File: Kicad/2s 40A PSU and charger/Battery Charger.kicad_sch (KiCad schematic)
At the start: 42 parts

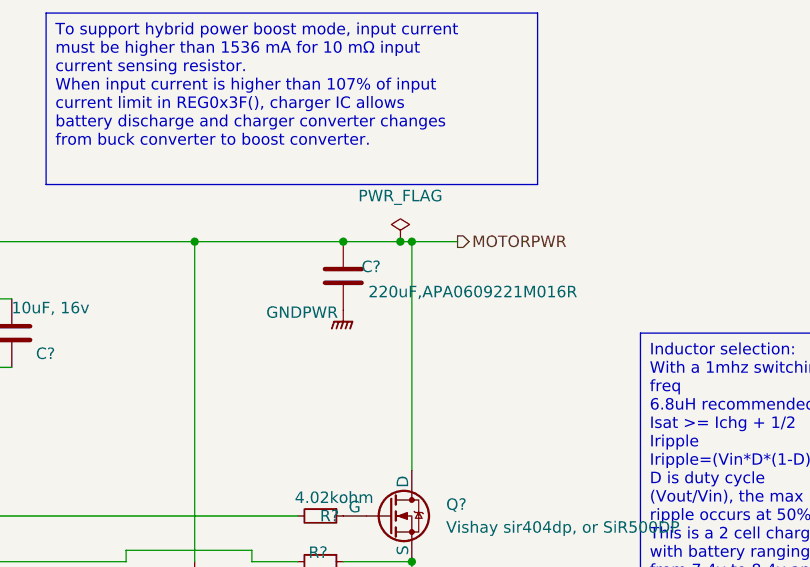
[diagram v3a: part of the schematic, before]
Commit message: Add proper ESD protection and pulldowns for USB-C
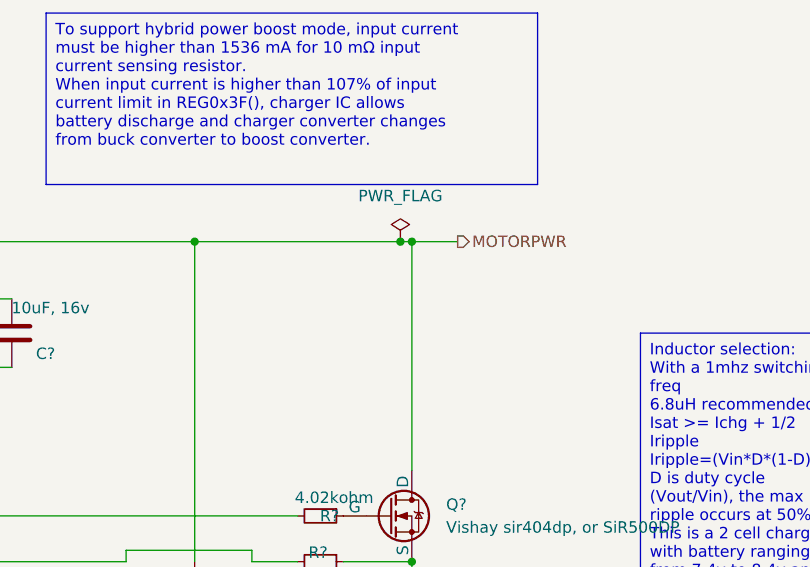
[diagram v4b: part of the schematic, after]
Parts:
- removed C?: 220uF,APA0609221M016R, Capacitor_SMD:CP_Elec_6.3x9.9, symbol Device:C
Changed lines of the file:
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@@
 	)
 	(junction
-		(at 193.04 54.61)
-		(diameter 0)
-		(color 0 0 0 0)
-	)
-	(junction
 		(at 200.66 107.95)
 		(diameter 0)
@@
 	(wire
 		(pts
-			(xy 176.53 54.61) (xy 193.04 54.61)
+			(xy 176.53 54.61) (xy 199.39 54.61)
 		)
 		(stroke
@@
 	(wire
 		(pts
-			(xy 199.39 54.61) (xy 193.04 54.61)
-		)
-		(stroke
-			(width 0)
-			(type default)
-		)
-	)
-	(wire
-		(pts
 			(xy 111.76 107.95) (xy 90.17 107.95)
 		)
@@
 	)
 	(symbol
-		(lib_id "power:GNDPWR")
-		(at 193.04 62.23 0)
-		(unit 1)
-		(exclude_from_sim no)
-		(in_bom yes)
-		(on_board yes)
-		(dnp no)
-		(property "Reference" "#PWR?"
-			(at 193.04 67.31 0)
-			(effects
-				(font
-					(size 1.27 1.27)
-				)
-				(hide yes)
-			)
-		)
-		(property "Value" "GNDPWR"
-			(at 188.468 62.484 0)
-			(effects
-				(font
-					(size 1.27 1.27)
-				)
-			)
-		)
-		(property "Footprint" ""
-			(at 193.04 63.5 0)
-			(effects
-				(font
-					(size 1.27 1.27)
-				)
-				(hide yes)
-			)
-		)
-		(property "Datasheet" ""
-			(at 193.04 63.5 0)
-			(effects
-				(font
-					(size 1.27 1.27)
-				)
-				(hide yes)
-			)
-		)
-		(property "Description" "Power symbol creates a global label with name \"GNDPWR\" , global ground"
-			(at 193.04 62.23 0)
-			(effects
-				(font
-					(size 1.27 1.27)
-				)
-				(hide yes)
-			)
-		)
-		(pin "1"
-		)
-		(instances
-			(project "Battery Charger"
-				(path "/a7feb2bd-883b-459c-b24f-35371efba833"
-					(reference "#PWR?")
-					(unit 1)
-				)
-			)
-			(project "2s 40A PSU and charger"
-				(path "/eb3f183d-8bb1-43a5-a363-092ed67891e3/51a1bb53-ba94-4dbc-a00c-ce32ffc237e4"
-					(reference "#PWR06")
-					(unit 1)
-				)
-			)
-		)
-	)
-	(symbol
 		(lib_id "Device:R_Small")
 		(at 190.5 85.09 270)
@@
 					(unit 1)
 				)
-			)
-		)
-	)
-	(symbol
-		(lib_id "Device:C")
-		(at 193.04 58.42 0)
-		(unit 1)
-		(exclude_from_sim no)
-		(in_bom yes)
-		(on_board yes)
-		(dnp no)
-		(property "Reference" "C?"
-			(at 195.072 57.404 0)
-			(effects
-				(font
-					(size 1.27 1.27)
-				)
-				(justify left)
-			)
-		)
-		(property "Value" "220uF,APA0609221M016R"
-			(at 195.834 60.198 0)
-			(effects
-				(font
-					(size 1.27 1.27)
-				)
-				(justify left)
-			)
-		)
-		(property "Footprint" "Capacitor_SMD:CP_Elec_6.3x9.9"
-			(at 194.0052 62.23 0)
-			(effects
-				(font
-					(size 1.27 1.27)
-				)
-				(hide yes)
-			)
-		)
-		(property "Datasheet" "~"
-			(at 193.04 58.42 0)
-			(effects
-				(font
-					(size 1.27 1.27)
-				)
-				(hide yes)
-			)
-		)
-		(property "Description" "Unpolarized capacitor"
-			(at 193.04 58.42 0)
-			(effects
-				(font
-					(size 1.27 1.27)
-				)
-				(hide yes)
-			)
-		)
-		(pin "1"
-		)
-		(pin "2"
-		)
-		(instances
-			(project "Battery Charger"
-				(path "/a7feb2bd-883b-459c-b24f-35371efba833"
-					(reference "C?")
-					(unit 1)
-				)
-			)
-			(project "2s 40A PSU and charger"
-				(path "/eb3f183d-8bb1-43a5-a363-092ed67891e3/51a1bb53-ba94-4dbc-a00c-ce32ffc237e4"
-					(reference "C7")
-					(unit 1)
-				)

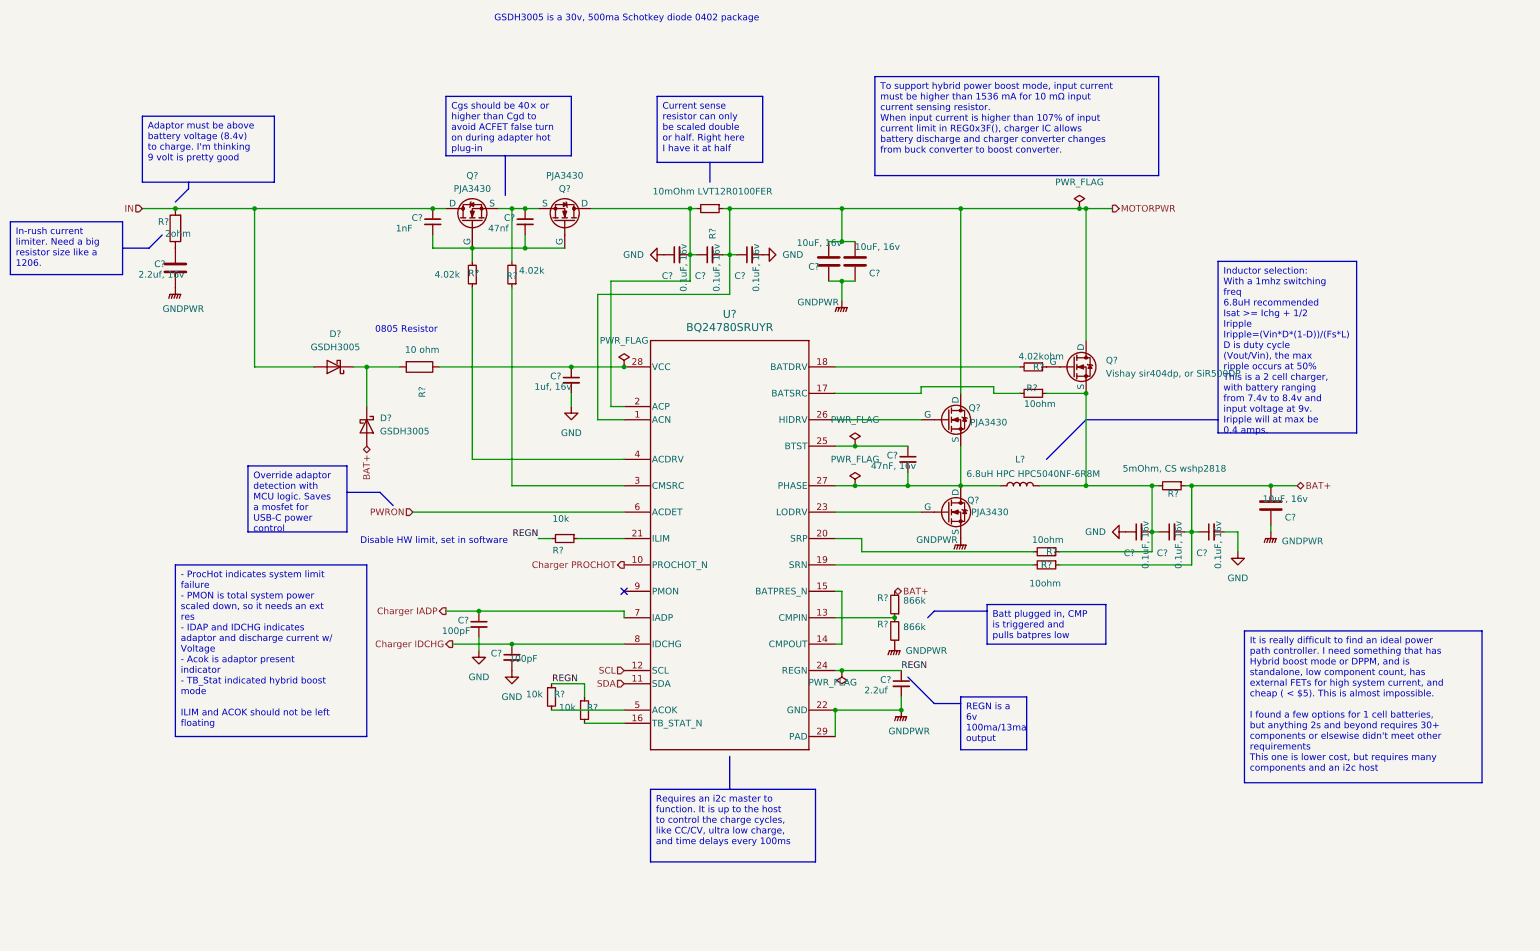
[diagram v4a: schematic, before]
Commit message: Added use of Net Class Directives to speed up routing
I don't have to manually change wire sizes now
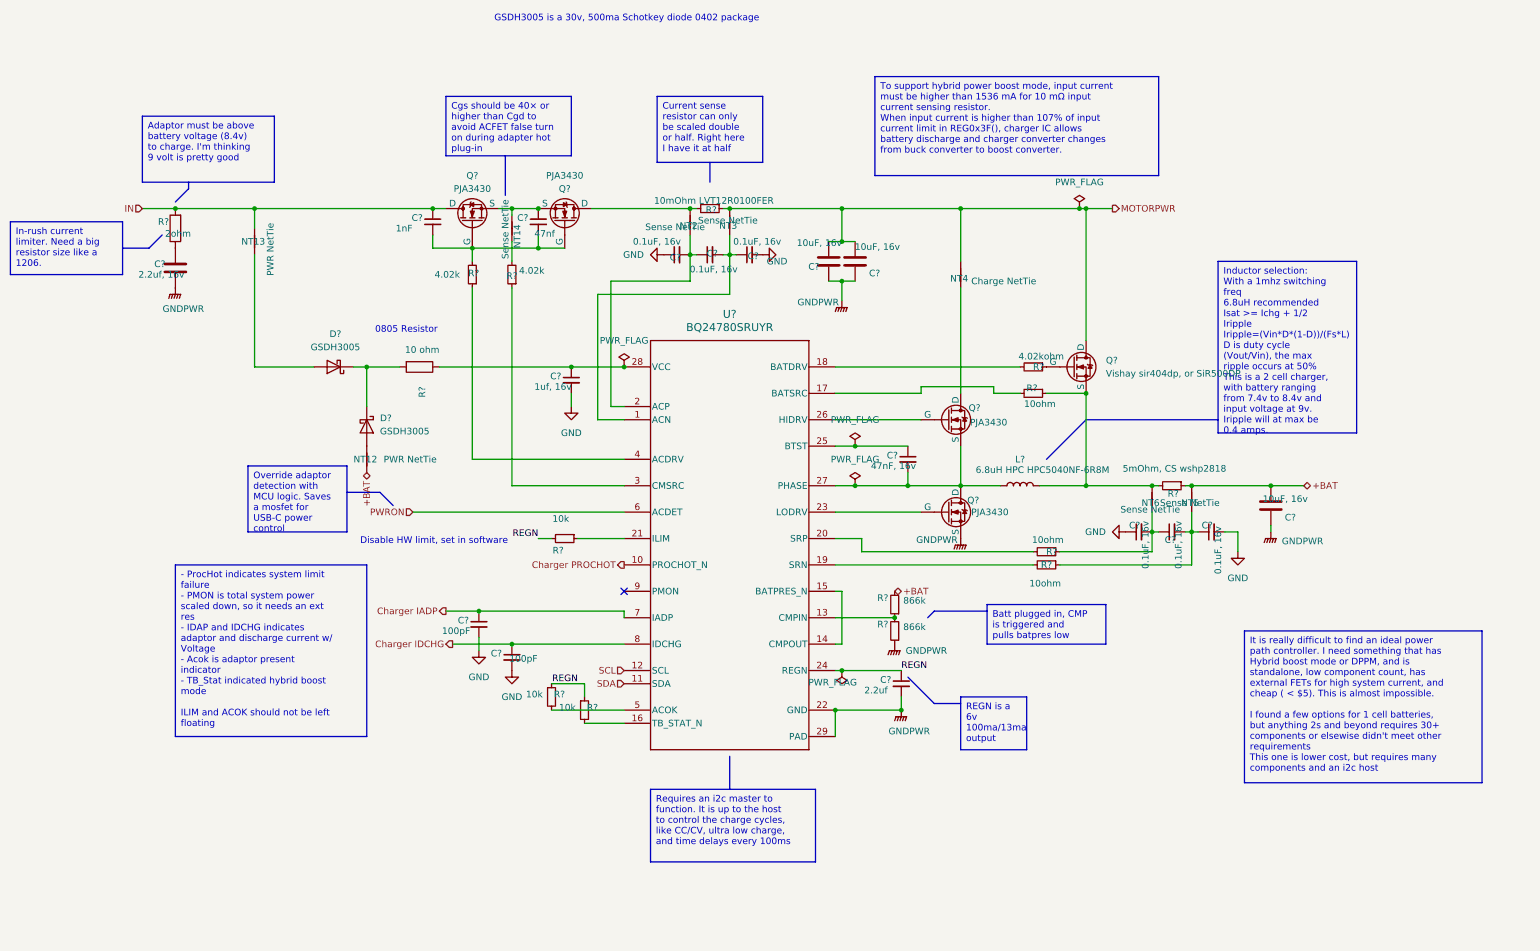
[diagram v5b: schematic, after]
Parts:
- added NT12, NT13: PWR NetTie, custom_Connector:NetTie-2_SMD_Pad0.28mm, symbol Device:NetTie_2
- added NT14, NT2, NT3, NT5, NT6: Sense NetTie, custom_Connector:NetTie-2_SMD_Pad0.16mm, symbol Device:NetTie_2
- added NT4: Charge NetTie, custom_Connector:NetTie-2_SMD_Pad0.8mm, symbol Device:NetTie_2
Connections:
- net IN: now also NT13.1; no longer D?.2 (A)
- net MOTORPWR: now also NT3.2, NT4.2; no longer C?.1, C?.2, Q?.1 (D), U?.1 (ACN)
- net at C?.1, Q?.3 (S), Q?.3 (S): now also NT14.2; no longer R?.2
- net at L?.2, Q?.5 (S), R?.1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: now also NT6.2; no longer C?.1, C?.2, R?.1
- net at C?.1, C?.2, U?.2 (ACP): now also NT2.1; no longer Q?.1 (D), R?.2
- removed net BAT+: C?.1, C?.2, C?.2, D?.2 (A), R?.1, R?.1, R?.2
- new net: C?.1, C?.2, NT5.1, R?.1
- new net: C?.1, C?.2, NT6.1, R?.1
- new net: D?.2 (A), NT13.2
- new net: C?.1, C?.2, NT3.1, U?.1 (ACN)
- new net: NT14.1, R?.2
- new net: D?.2 (A), NT12.1
- new net: NT2.2, Q?.1 (D), R?.2
- new net: NT4.1, Q?.1 (D)
- new net +BAT: C?.2, NT12.2, NT5.2, R?.1, R?.2
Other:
- moved on the sheet: C?

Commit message: Updated Sheet Properties
My author name is now in there, and I've added the proper project name.
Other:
- title: (none) -> CACKLE 2s 40A PSU & Charger
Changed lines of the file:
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@@
 	(paper "A4")
 	(title_block
-		(date "2024-11-28")
-		(rev "V1 Alpha")
+		(title "CACKLE 2s 40A PSU & Charger")
+		(date "2024-12-01")
+		(rev "V1")
+		(comment 1 "Author: Asher Edwards")
 	)
 	(junction

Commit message: Changed battery input pads to through holes with vias
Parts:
- NT14, NT2, NT3, NT5, NT6: footprint custom_Connector:NetTie-2_SMD_Pad0.16mm -> custom_Connector:NetTie-2_SMD_Pad0.2mm
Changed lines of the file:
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@@
 			)
 		)
-		(property "Footprint" "custom_Connector:NetTie-2_SMD_Pad0.16mm"
+		(property "Footprint" "custom_Connector:NetTie-2_SMD_Pad0.2mm"
 			(at 220.98 110.49 0)
 			(effects
@@
 			)
 		)
-		(property "Footprint" "custom_Connector:NetTie-2_SMD_Pad0.16mm"
+		(property "Footprint" "custom_Connector:NetTie-2_SMD_Pad0.2mm"
 			(at 213.36 110.49 0)
 			(effects
@@
 			)
 		)
-		(property "Footprint" "custom_Connector:NetTie-2_SMD_Pad0.16mm"
+		(property "Footprint" "custom_Connector:NetTie-2_SMD_Pad0.2mm"
 			(at 90.17 58.42 0)
 			(effects
@@
 			)
 		)
-		(property "Footprint" "custom_Connector:NetTie-2_SMD_Pad0.16mm"
+		(property "Footprint" "custom_Connector:NetTie-2_SMD_Pad0.2mm"
 			(at 132.08 57.15 0)
 			(effects
@@
 			)
 		)
-		(property "Footprint" "custom_Connector:NetTie-2_SMD_Pad0.16mm"
+		(property "Footprint" "custom_Connector:NetTie-2_SMD_Pad0.2mm"
 			(at 124.46 57.15 0)
 			(effects

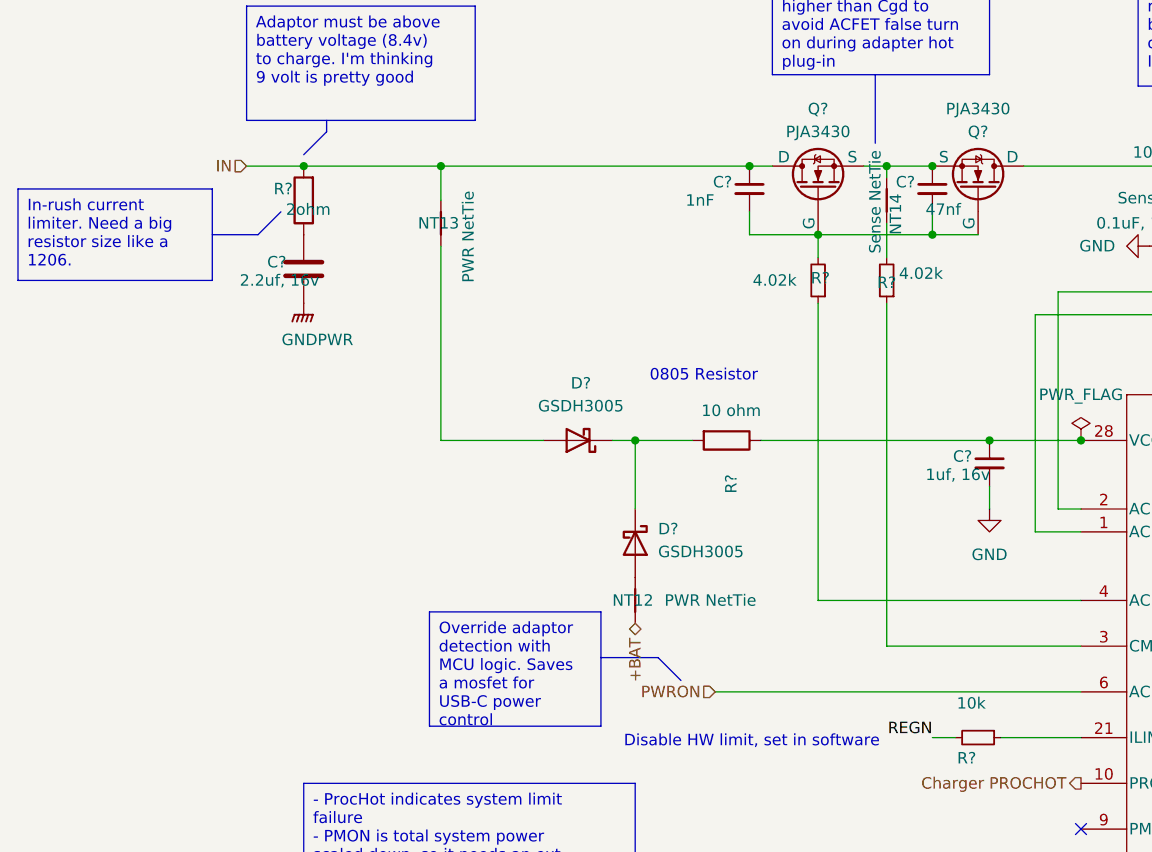
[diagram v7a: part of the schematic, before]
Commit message: Merged Always on PWR for multiple devices
The diode OR and the 10 ohm resistor are now shared between the MCU and the battery charger
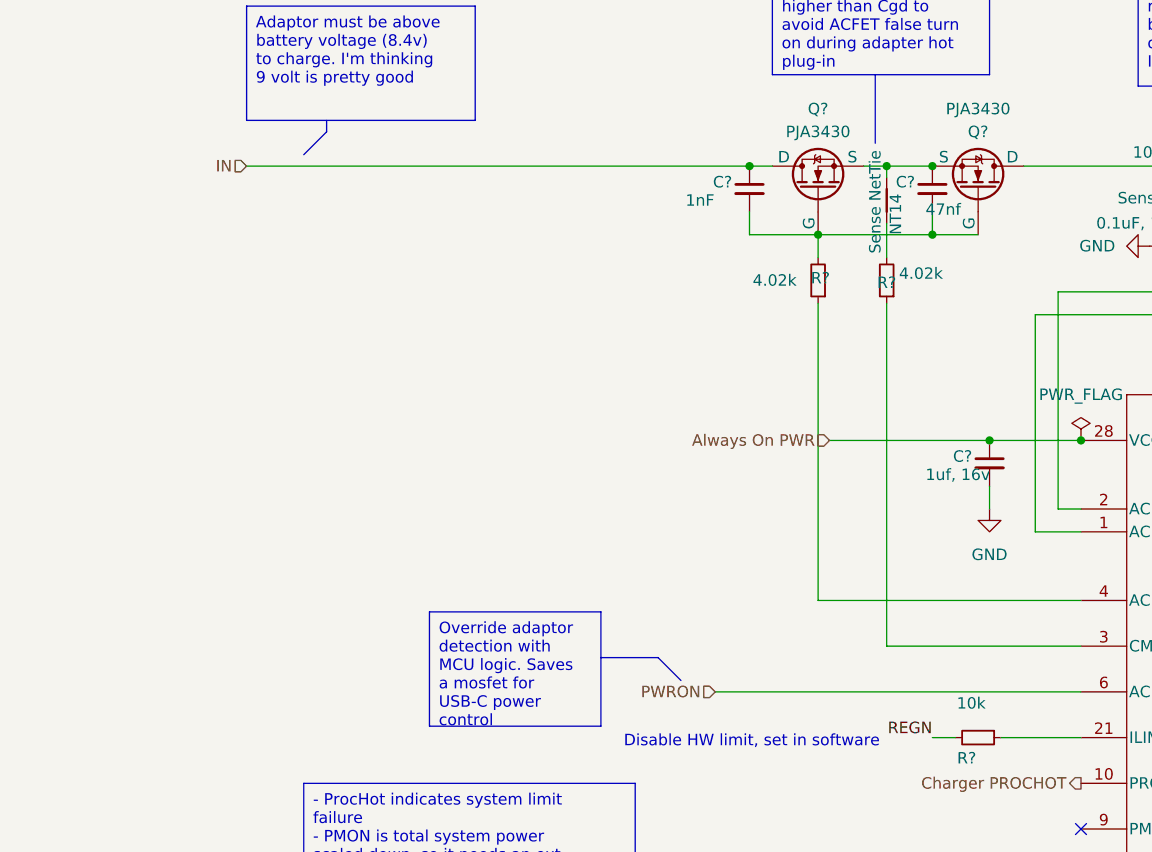
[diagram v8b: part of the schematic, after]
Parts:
- removed C?: 2.2uf, 16v, Capacitor_SMD:C_1206_3216Metric, symbol Device:C
- removed D? (x2): GSDH3005, Diode_SMD:D_0402_1005Metric, symbol Device:D_Schottky
- removed NT12, NT13: PWR NetTie, custom_Connector:NetTie-2_SMD_Pad0.28mm, symbol Device:NetTie_2
- removed R?: 2ohm, Resistor_SMD:R_1206_3216Metric, symbol Device:R
- removed R?: 10 ohm, Resistor_SMD:R_0805_2012Metric, symbol Device:R
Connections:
- net Always On PWR: now reaches C?.1, U?.28 (VCC)
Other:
- note removed: "0805 Resistor"
